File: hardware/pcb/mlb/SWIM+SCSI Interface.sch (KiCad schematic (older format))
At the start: 25 parts, among them J4 DB-25, J5 SCSI, J6 DB-19, J8 Ribbon Connector

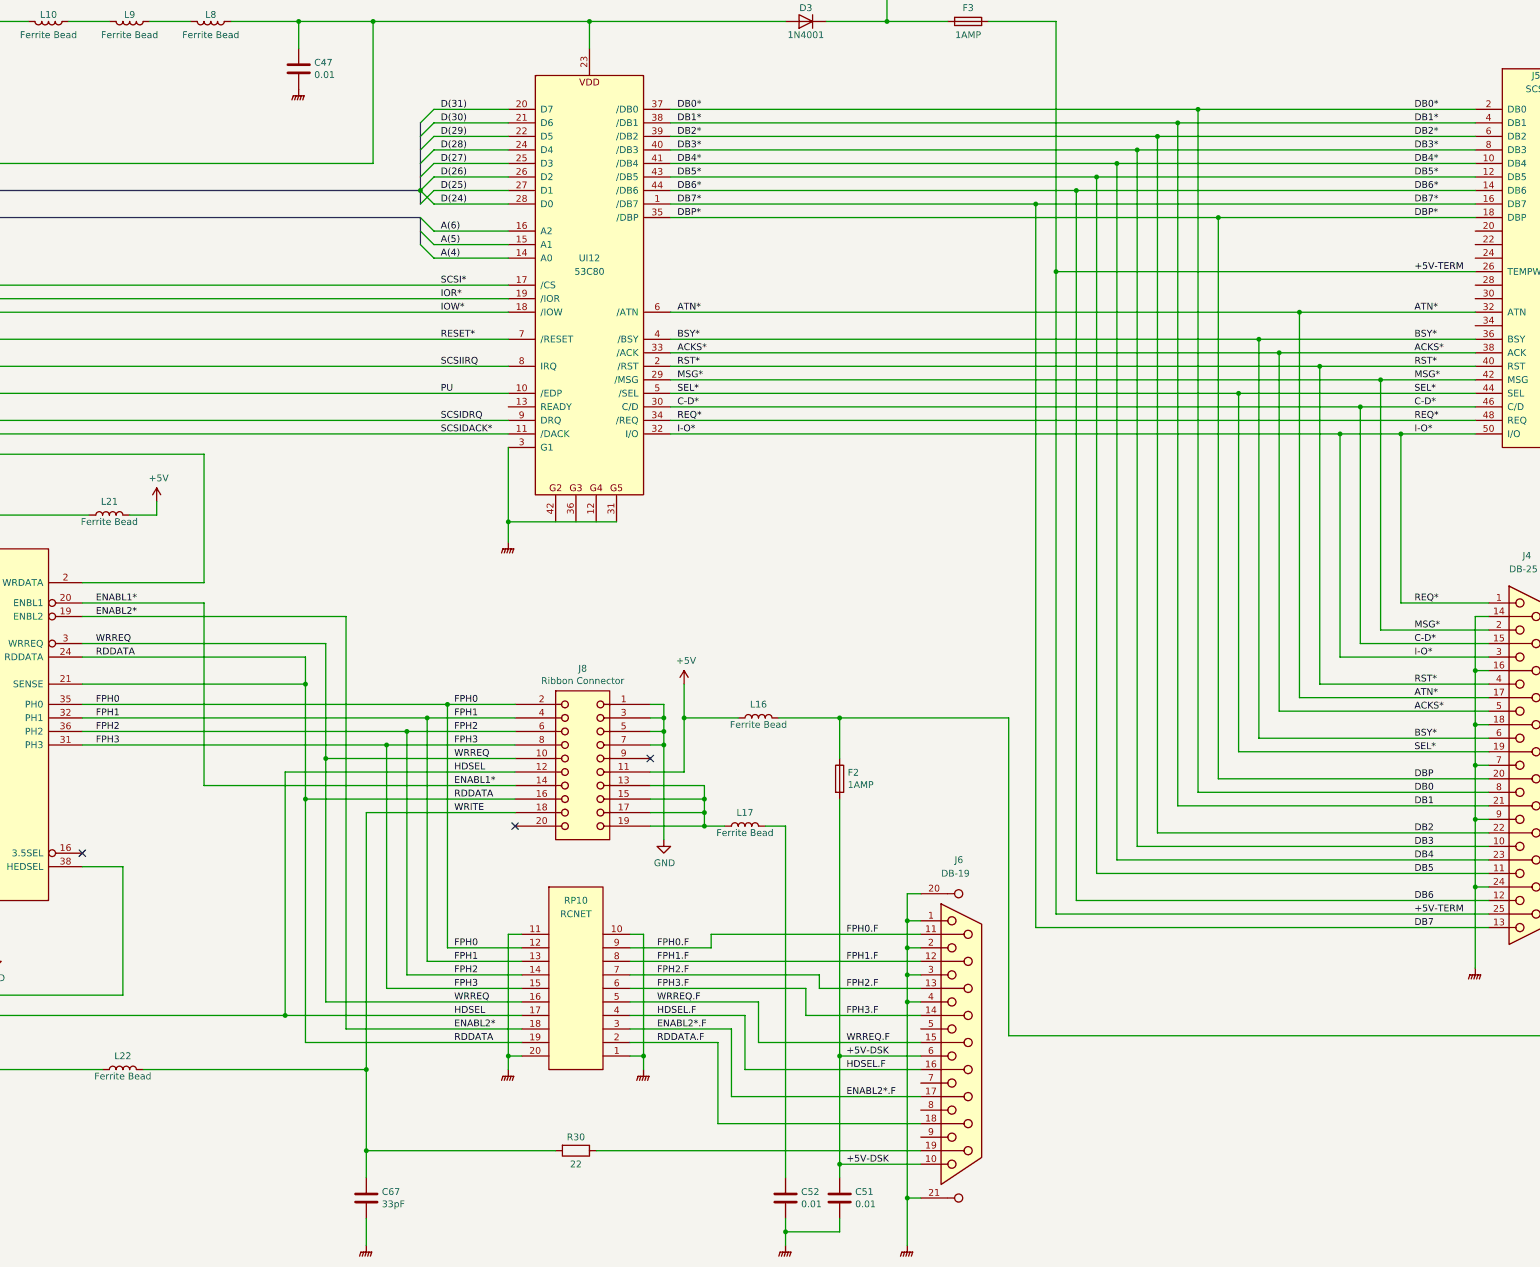
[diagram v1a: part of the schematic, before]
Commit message: Fix errors found in review of the Macintosh SE/30 schematic redraw.
Page 1:

* DSACK*(0:1) (syntax)
* R-W* (inconsistent syntax)
* IPL different syntax
* PDS 38, C16M not grounded
* PDS 39, should be grounded

Page 2:

* RAAF*(8), RABF*(9), RAAF*(10), RABF*(10) (syntax)
* RCMUX* (syntax)
* ROM* missing page 3 indicator
* ROMSIMM1 GND 10, 30, 64
* ROMSIMM1 Incorrect +5V lines
* ROMSIMM1 Confusing bus line drawing angles makes connections look
  duplicated

Page 3:

* VIAIRQ2* (syntax)
* VIAIRQ1N (syntax, on GLUE template)
* SCCRD* (syntax)

Page 4:

* VIA template, RS0, RS1, RS2, RS3 erroneously written as R50, R51,
  R52, R53
* V1PB7 erroneously written as VIPB7
* RTC-D erroneously written as RTC-O
* V1PA0, V1PA1, V1PA2 erroneously written as VIPA0, VIPA1, VIPA2
* warning: additional label BATT not present
* UL11 ADB template, P5 erroneously written as P2
* ADBO erroneously written as ADB0
* SNDINT* erroneously written as SNTINT*

Page 5:

* HSYNC* on UG7 (syntax)
* UJ6 confusing bus line makes signals look duplicated
* Video ROM UK6 not labeled with reference designator (already inside
  KiCad file, stale PDF?)
* VIDS4, VIDS3, VIDS2, VIDS1, VIDS0 erroneously written a VID54,
  VID53, VID53, VID51, VID50
* R-W* alternate page reference erroneously written as RW*
* 74F253 template, G erroneously labeled as GND
* 74F253 template, missing second G enable pin
* style: C0 in 74F253 template should not be C0(GND)
* warning: UA8 ALTVID line could have another label close to the chip

Page 6:

* warning: On SWIM, WRDATA could have label WR*
* DB25 connector: DP*, DB0*, DB1*, DB2*, DB3*, DB4*, DB5*, DB6*, DB7*
  (syntax)
* J8 Ribbon Connector: Missing +12V on 13, 15, 17, 19
* J6 DB-19: Missing +12V-DSK on 7, 8
* warning: missing RDDATA.F additional label near J6 DB-19 pin 18
* warning: missing WRITE.F additional label near J6 DB-19 pin 19
* warning: confusing bus line layout on 53C80 looks like duplicate
  wiring

Page 7:

* RXDA+ erroneously written as RXDB+
* HSKOA erroneo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
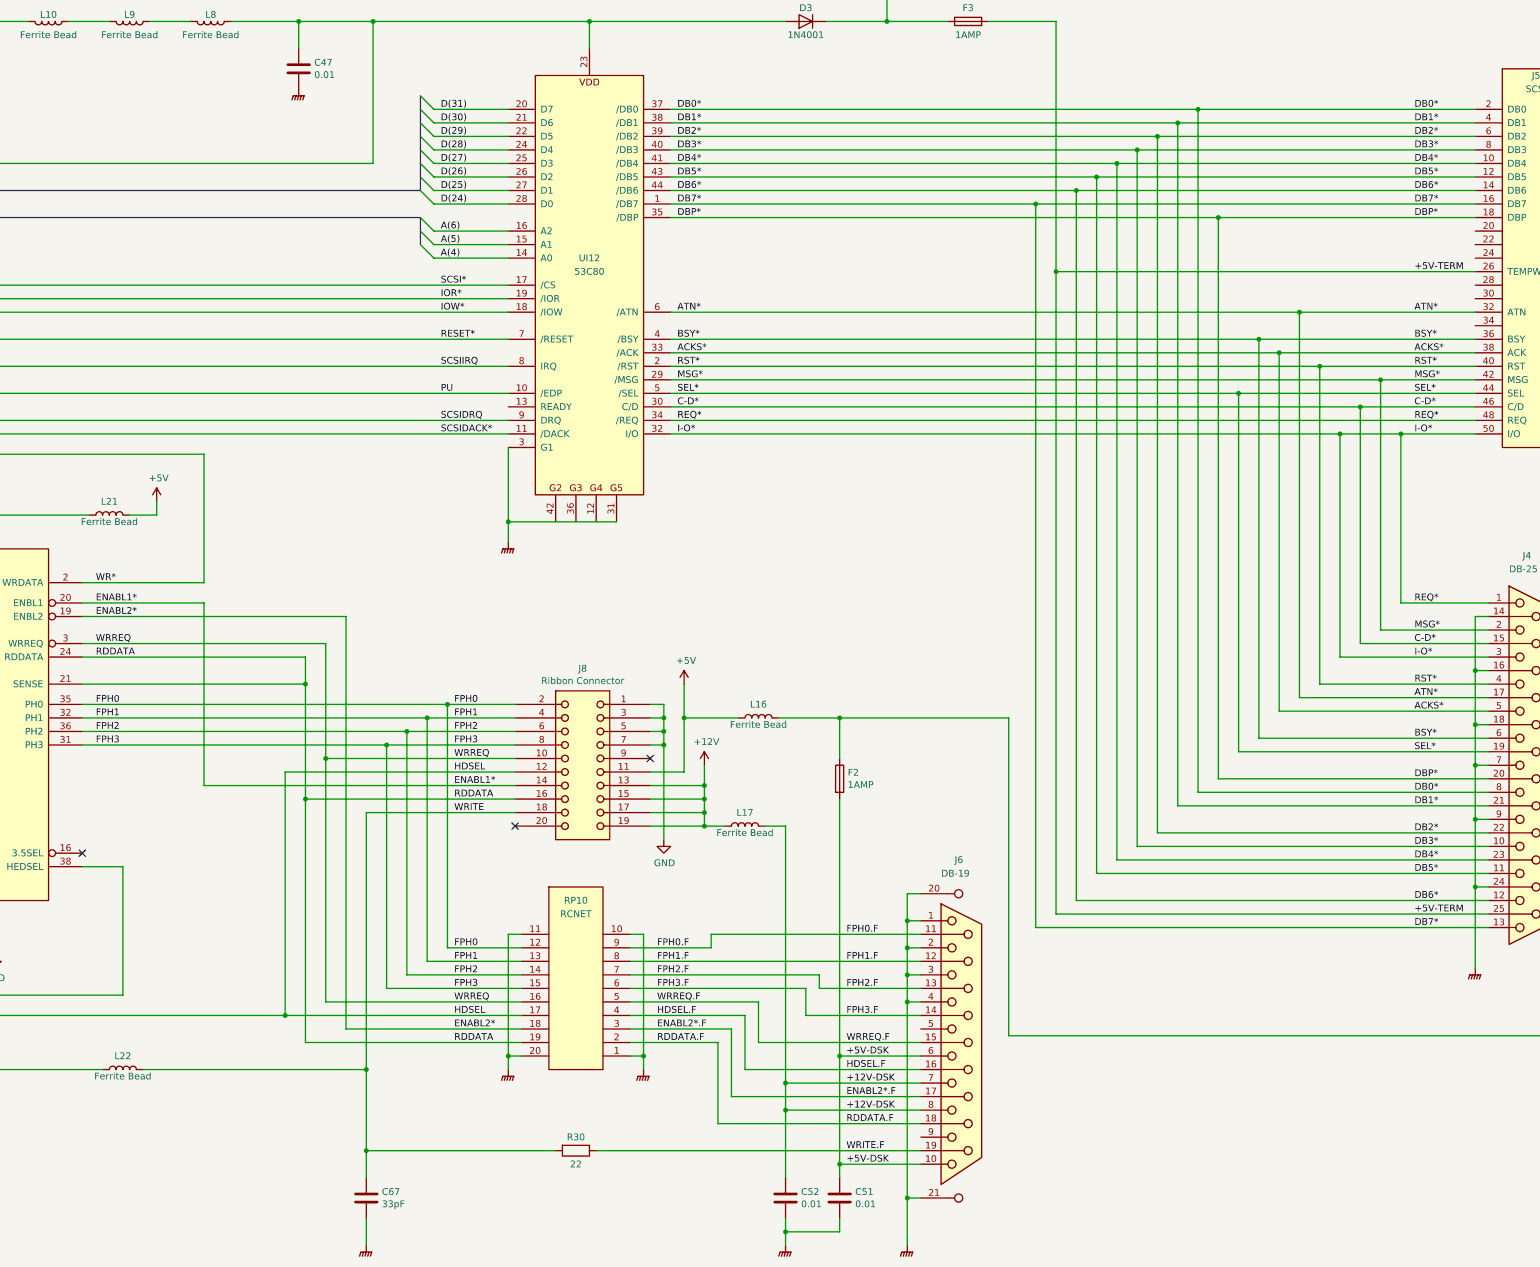
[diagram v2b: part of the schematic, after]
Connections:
- net WRITE.F: now reaches J6.19 (P19), R30.1
- net +12V-DSK: now reaches J6.7
- net +12V-DSK: now also C52.1, J6.8, L17.2
- net +12V: now reaches J8.13, J8.15, J8.17, J8.19, L17.1
- net DB0 renamed DB0*
- net DB1 renamed DB1*
- net DB2 renamed DB2*
- net DB3 renamed DB3*
- net DB4 renamed DB4*
- net DB5 renamed DB5*
- net DB6 renamed DB6*
- net DB7 renamed DB7*
- net DBP renamed DBP*
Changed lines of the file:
@@
 Connection ~ 12600 2700
 Text Label 14050 6850 0    50   ~ 0
-DBP
+DBP*
 Wire Wire Line
 	14600 6950 12450 6950
@@
 Connection ~ 12450 1900
 Text Label 14050 6950 0    50   ~ 0
-DB0
+DB0*
 Wire Wire Line
 	14600 7050 12300 7050
@@
 	12300 2000 14500 2000
 Text Label 14050 7050 0    50   ~ 0
-DB1
+DB1*
 Wire Wire Line
 	14600 7250 12150 7250
@@
 Connection ~ 12150 2100
 Text Label 14050 7250 0    50   ~ 0
-DB2
+DB2*
 Wire Wire Line
 	14600 7350 12000 7350
@@
 	12000 2200 14500 2200
 Text Label 14050 7350 0    50   ~ 0
-DB3
+DB3*
 Wire Wire Line
 	14600 7450 11850 7450
@@
 Connection ~ 11850 2300
 Text Label 14050 7450 0    50   ~ 0
-DB4
+DB4*
 Wire Wire Line
 	14600 7550 11700 7550
@@
 	11700 2400 14500 2400
 Text Label 14050 7550 0    50   ~ 0
-DB5
+DB5*
 Wire Wire Line
 	11550 7750 11550 2500
 Connection ~ 11550 2500
 Text Label 14050 7750 0    50   ~ 0
-DB6
+DB6*
 Wire Wire Line
 	11400 7850 11400 3100
@@
 +5V-TERM
 Text Label 14050 7950 0    50   ~ 0
-DB7
+DB7*
 Wire Wire Line
 	8550 3400 13200 3400
@@
 $EndComp
 Wire Wire Line
-	9400 7200 9400 9800
+	9400 7200 9400 9100
 Wire Wire Line
 	9800 9700 9800 9800
@@
 Connection ~ 1950 2700
 Entry Wire Line
-	6800 2600 6700 2500
+	6800 2500 6700 2400
 Entry Wire Line
-	6800 2500 6700 2600
+	6800 2400 6700 2300
 Entry Wire Line
-	6800 2400 6700 2500
+	6800 2300 6700 2200
 Entry Wire Line
-	6800 2300 6700 2400
+	6800 2200 6700 2100
 Entry Wire Line
-	6800 2200 6700 2300
+	6800 2100 6700 2000
 Entry Wire Line
-	6800 2100 6700 2200
+	6800 2000 6700 1900
 Entry Wire Line
-	6800 2000 6700 2100
-Entry Wire Line
-	6800 1900 6700 2000
+	6800 1900 6700 1800
 Entry Wire Line
 	1900 6900 1800 6800
@@
 	6700 2500 1800 2500
 Connection ~ 1800 2500
-Wire Bus Line
-	6700 2600 6700 2500
-Connection ~ 6700 2500
 Text Notes 910  2335 2    50   ~ 0
 (9)
@@
 Wire Wire Line
 	3450 8000 3550 8000
+Text Label 4300 5400 0    50   ~ 0
+WR*
+$Comp
+L power:+12V #PWR?
+U 1 1 606738BC
+P 8800 6750
+F 0 "#PWR?" H 8800 6600 50  0001 C CNN
+F 1 "+12V" H 8815 6923 50  0000 C CNN
+F 2 "" H 8800 6750 50  0001 C CNN
+F 3 "" H 8800 6750 50  0001 C CNN
+	1    8800 6750
+	1    0    0    -1
+$EndComp
+Wire Wire Line
+	8800 6750 8800 6900
+Connection ~ 8800 6900
+Wire Wire Line
+	10400 9100 9400 9100
+Connection ~ 9400 9100
+Wire Wire Line
+	9400 9100 9400 9300
+Wire Wire Line
+	10400 9300 9400 9300
+Connection ~ 9400 9300
+Wire Wire Line
+	9400 9300 9400 9800
+Text Label 9850 9100 0    50   ~ 0
++12V-DSK
+Text Label 9850 9300 0    50   ~ 0
++12V-DSK
+Entry Wire Line
+	6800 2600 6700 2500
 Wire Bus Line
 	6700 2700 6700 2900
@@
 	1950 2700 1950 5900
 Wire Bus Line
-	6700 2000 6700 2500
+	6700 1800 6700 2500
 Wire Bus Line
 	1800 2500 1800 6800
+Text Label 9850 9400 0    50   ~ 0
+RDDATA.F
+Text Label 9850 9600 0    50   ~ 0
+WRITE.F
 $EndSCHEMATC
